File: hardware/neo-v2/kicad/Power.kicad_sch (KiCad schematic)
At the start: 75 parts, among them SW3 MK-12C02 G1.5, U10 TPS62827DMQR, U11 ME6211C18M5G-N, U12 TPS62065DSGR, U13 SGM2594BDXN5G/TR, U17 SGM7222YWQ10/TR

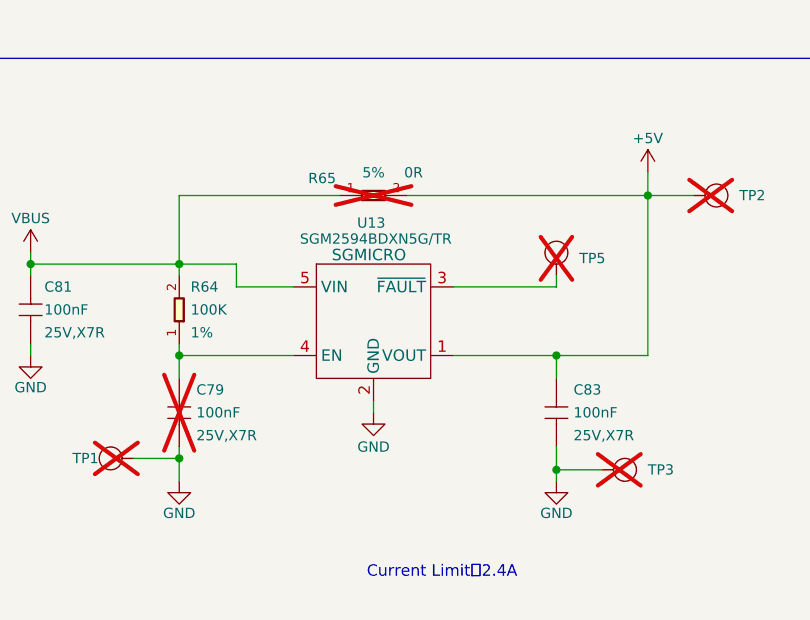
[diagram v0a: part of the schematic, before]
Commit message: hardware(neo-v2): fase 3, esquemático de bloques nuevos e integración
- Hojas nuevas Alimentacion (TPS2121, TPS61022, BQ25170, MAX17048,
  DW01A + 2x FS8205A, CSD25402Q3A, interruptor) y Expansion (conector
  OLED, pull-ups I2C, puntos de prueba), generadas por script desde
  tablas pin -> neta, referencias 201-235.
- Hojas heredadas: elimina U13 y el puerto Grove, reasigna GPIO1/2/46
  y deja sin montar R83, R84, R91 y R135; limpia hilos sueltos.
- Biblioteca propia de símbolos y huellas verificada contra los planos
  del fabricante y la huella de LCSC.
- Verificación formal de netlist contra el original y contra la
  conectividad prevista; ERC sin avisos en las hojas nuevas.
- Documentación, BOM de bloques nuevos, CHANGES.md y PDF del esquemático.

Co-Authored-By: Claude Opus 5.5 <noreply@anthropic.com>
Claude-Session: https://claude.ai/code/session_01UWwWJAyCeb1aBHbGbkDaMx
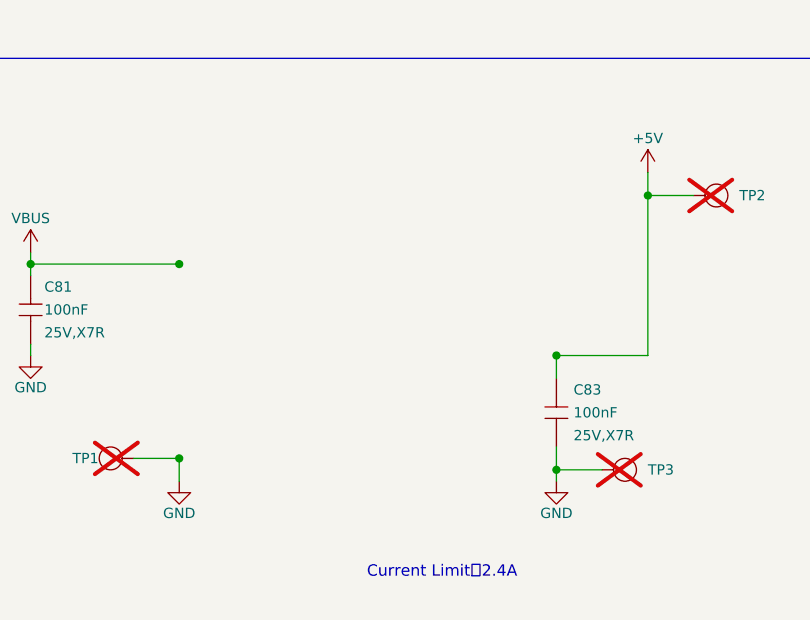
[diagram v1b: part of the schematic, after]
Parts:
- removed C79: 100nF, Capacitor:C0402, symbol Seeed_libadl:Capacitors/302010024
- removed R64: 100K, Resistor:R0402, symbol Seeed_libadl:Resistors/301010456
- removed R65: 0R, Resistor:R1206, symbol Seeed_libadl:Resistors/301010407
- removed TP5: TEST-POINT, Seeed_Misc:TP-D45MIL, symbol 0_Seeed_Misc:TEST-POINT
- removed U13: SGM2594BDXN5G/TR, Seeed_Ic:SOT-23-5, symbol reSpeaker:SGM2588CYN5GTR

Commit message: NEO v2 fase 5 (en curso): ERC sin errores y ruteo de potencia
- ERC: anotaciones PWR_FLAG / no conexión sobre las hojas heredadas
  (tools/erc_annotations.py); 0 errores, solo los avisos del original.
- PCB: elevador recolocado (lazo caliente mínimo), grupo de U201 ajustado,
  ranura de SW3 estrechada y prioridad de zonas de ANT2 corregida;
  la región de rehacer de U13 conserva el VBUS de F.Cu.
- Ruteo manual de potencia (tools/route_power.py): batería, PACK_P,
  nodo SW, salida del elevador, diodo ideal, protección y U201.
- Herramientas para el autorruteo con Freerouting, cosido de GND y
  exclusiones de DRC heredadas (pendientes de aplicar).

Estado intermedio: faltan las conexiones de señal (autorruteo).

Co-Authored-By: Claude Opus 5.5 <noreply@anthropic.com>
Claude-Session: https://claude.ai/code/session_01UWwWJAyCeb1aBHbGbkDaMx
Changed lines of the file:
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@@
 		)
 	)
+	(symbol (lib_id "power:PWR_FLAG") (at 87.63 78.74 0) (unit 1) (exclude_from_sim no) (in_bom no) (on_board yes) (dnp no)
+		(property "Reference" "#FLG911" (at 87.63 78.74 0) (effects (font (size 1.27 1.27)) (hide yes)))
+		(property "Value" "PWR_FLAG" (at 87.63 74.93 0) (effects (font (size 1.27 1.27))))
+		(property "Footprint" "" (at 87.63 78.74 0) (effects (font (size 1.27 1.27)) (hide yes)))
+		(property "Datasheet" "" (at 87.63 78.74 0) (effects (font (size 1.27 1.27)) (hide yes)))
+		(property "Description" "NEO v2 fase 5: anotación de ERC (#PWR0155)" (at 87.63 78.74 0) (effects (font (size 1.27 1.27)) (hide yes)))
+		(pin "1")
+		(instances (project "NEO_v2" (path "/349ed1f3-025e-4f39-9714-d91e135a7151/cee6f4f6-7555-4cac-941e-fc825fe0305c" (reference "#FLG911") (unit 1))))
+	)
 )
